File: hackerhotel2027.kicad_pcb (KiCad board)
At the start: 2 copper layers, 20 parts, among them J1 USB device, J2 USB host, U2 TPD4E05U06DQAR, Y1 32.768KHz

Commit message: Fill out all component LCSC numbers and fix footprint associations
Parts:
- removed C31: 100n, Capacitor_SMD:C_0402_1005Metric
- added C36: 4.7uF, Capacitor_SMD:C_0603_1608Metric, F.Cu at (174.6, 71.3)
- added C37: 1uF, Capacitor_SMD:C_0603_1608Metric, F.Cu at (174.6, 73.8)
- added C38: 1uF, Capacitor_SMD:C_0603_1608Metric, F.Cu at (174.6, 76.3)
- added C39: 1uF, Capacitor_SMD:C_0603_1608Metric, F.Cu at (174.6, 78.8)
- added C40: 1uF, Capacitor_SMD:C_0603_1608Metric, F.Cu at (174.6, 81.3)
- added C41: 1uF, Capacitor_SMD:C_0603_1608Metric, F.Cu at (178.6, 71.3)
- added C42: 1uF, Capacitor_SMD:C_0603_1608Metric, F.Cu at (178.6, 73.8)
- added C43: 1uF, Capacitor_SMD:C_0603_1608Metric, F.Cu at (178.6, 76.3)
- added C44: 1uF, Capacitor_SMD:C_0603_1608Metric, F.Cu at (178.6, 78.8)
- added C45: 470nF, Capacitor_SMD:C_0603_1608Metric, F.Cu at (178.6, 81.3)
- added D3: B0530WS, Diode_SMD:D_SOD-323, F.Cu at (187.3, 75.7)
- added D5: B0530WS, Diode_SMD:D_SOD-323, F.Cu at (187.3, 78.7)
- added D8: B0530WS, Diode_SMD:D_SOD-323, F.Cu at (187.3, 81.6)
- added FPC1: GT-F0501SR10-24S1101, lcsc:FPC-SMD_24P-P0.50_GT-F0501SR10-24S1101, F.Cu at (180.1, 67.0)
- added L1: 1.8n, Inductor_SMD:L_01005_0402Metric, F.Cu at (192.6, 69.4)
- added L9: 47uH, Inductor_SMD:L_1210_3225Metric, F.Cu at (183.4, 72.1)
- added Q2: AP2302B, lcsc:SOT-23-3_L2.9-W1.3-P1.90-LS2.4-BR, F.Cu at (182.8, 76.5)
- added R11: 2.2, Resistor_SMD:R_0805_2012Metric, F.Cu at (182.8, 80.2)
- added R12: 100k, Resistor_SMD:R_0402_1005Metric, F.Cu at (187.7, 71.0)
- added R13: 0, Resistor_SMD:R_0402_1005Metric, F.Cu at (187.7, 73.0)
- added U1: CH32V208CBU6_C5713556, ch32v208:QFN-48_L5.0-W5.0-P0.35-BL-EP-A, F.Cu at (209.1, 95.7)
- added Y2: 32MHz, Crystal:Crystal_SMD_3225-4Pin_3.2x2.5mm, F.Cu at (194.1, 66.3)
- C1, C2: value 22p -> 9p
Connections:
- J1 pad SH: (no net) -> GND

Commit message: Small tweaks & initial PCB work
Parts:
- AE2, C1, C2, C3, C32, C33, C34, C35, C36, C37, C38, C39, C4, C40, C41, C42, C43, C44, C45, C5, C6, C7, D3, D5, D8, FPC1, J1, J2, L1, L9, Q2, R1, R11, R12, R13, R2, R25, U1, U2, Y1, Y2: moved to B.Cu
- moved U1 235.6 mm to (3.88, -20.1), turned to 180 degrees
- moved R12 210.9 mm to (-9.88, -2.77), turned to 180 degrees
- moved L1 209.6 mm to (5.45, -25.0), turned to 90 degrees
- moved R11 208.8 mm to (-10.9, 2.23), turned to 180 degrees
- moved Y2 206.3 mm to (4.00, -14.0), turned to 180 degrees
- moved Q2 204.5 mm to (-4.88, -4.78), turned to 180 degrees
- moved C41 202.7 mm to (-10.9, -0.78), turned to 180 degrees
- moved D8 201.2 mm to (5.12, -3.77), turned to 180 degrees
- moved L9 198.8 mm to (0.12, -4.78), turned to 180 degrees
- moved R13 197.8 mm to (0.12, 10.2), turned to 180 degrees
- moved C36 197.6 mm to (2.00, -25.0), turned to 180 degrees
- moved C40 196.8 mm to (-6.88, 5.22), turned to 180 degrees
- moved J1 195.6 mm to (-32.0, 0.00), turned to 90 degrees
- moved R2 194.5 mm to (-25.0, 0.00), turned to 180 degrees
- moved D3 193.5 mm to (9.12, 0.23), turned to 180 degrees
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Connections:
- net BTN1 renamed PWR_BTN
- net BTN2 renamed T1
- U1 pad 11: unconnected-(U1-PA2/ADC2-Pad11) -> T2
- U1 pad 12: unconnected-(U1-PA3/ADC3-Pad12) -> T3
- U1 pad 13: unconnected-(U1-PA4/ADC4-Pad13) -> T4
- U1 pad 14: SPI_SCK -> T5
- U1 pad 15: SPI_MISO -> T6
- U1 pad 16: SPI_MOSI -> T7
- U1 pad 17: unconnected-(U1-PB0/ADC8-Pad17) -> T8
- U1 pad 18: unconnected-(U1-PB1/ADC9-Pad18) -> T9
- U1 pad 20: unconnected-(U1-PB10-Pad20) -> I2C2_SCL
- U1 pad 21: unconnected-(U1-PB11-Pad21) -> I2C2_SDA
- U1 pad 23: unconnected-(U1-PB12-Pad23) -> EPAPER_BUSY
- U1 pad 24: unconnected-(U1-PB13-Pad24) -> SPI_SCK
- U1 pad 25: unconnected-(U1-PB14-Pad25) -> SPI_MISO
- U1 pad 26: unconnected-(U1-PB15-Pad26) -> SPI_MOSI
- U1 pad 27: unconnected-(U1-PA8-Pad27) -> SPI_CS_EPAPER
- U1 pad 28: unconnected-(U1-PA9-Pad28) -> SPI_CS_FLASH
- U1 pad 29: unconnected-(U1-PA10-Pad29) -> EPAPER_DC
- U1 pad 37: unconnected-(U1-PA15-Pad37) -> LM4
- U1 pad 38: unconnected-(U1-PB3-Pad38) -> LM3
- U1 pad 39: unconnected-(U1-PB4-Pad39) -> LM2
- U1 pad 40: unconnected-(U1-PB5-Pad40) -> LM1
- U1 pad 43: unconnected-(U1-BOOT0-Pad43) -> BOOT
- U1 pad 44: unconnected-(U1-PB8-Pad44) -> I2C1_SCL
- U1 pad 45: unconnected-(U1-PB9-Pad45) -> I2C1_SDA
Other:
- board outline added: 70 x 70 mm

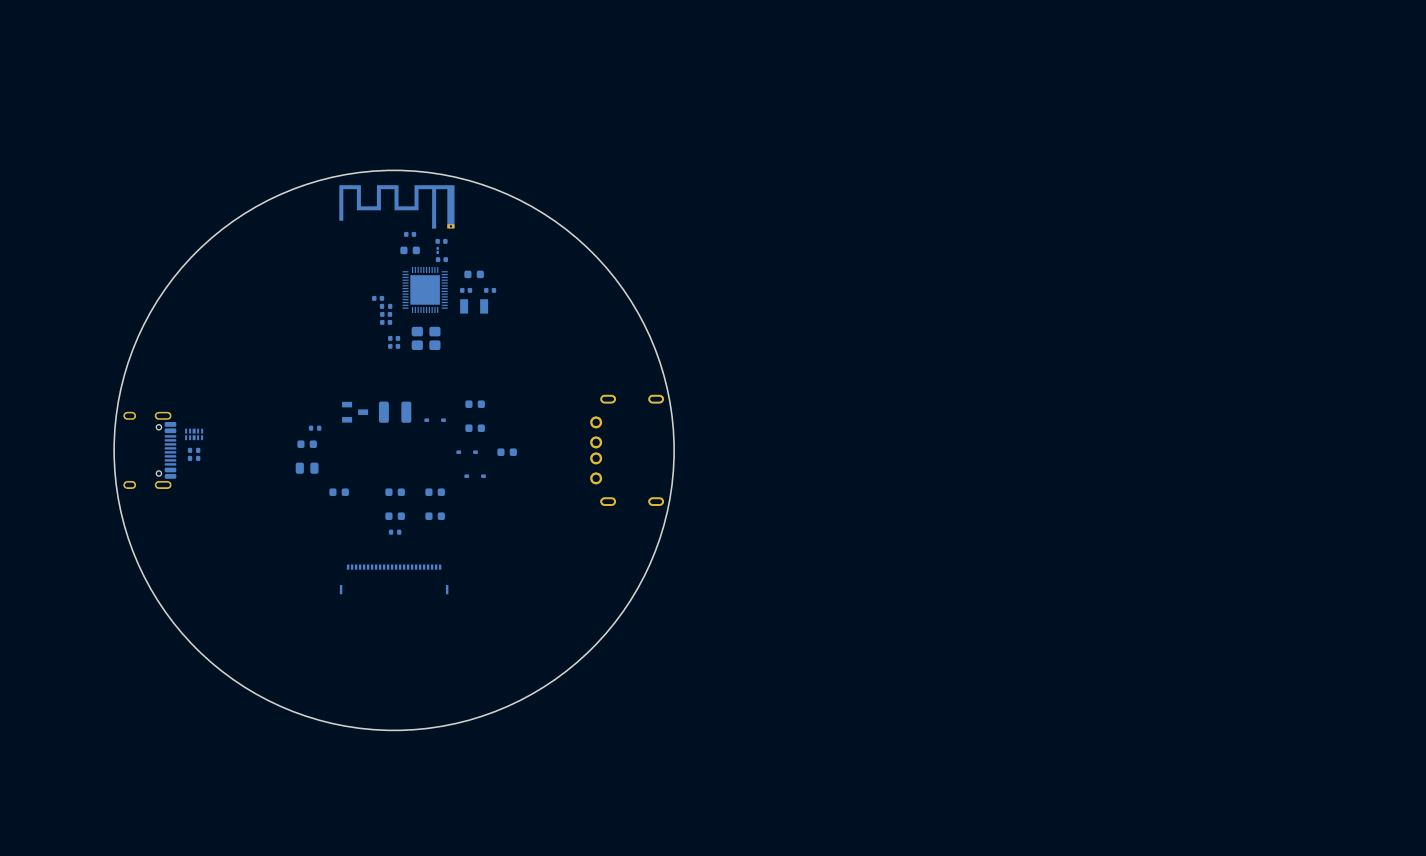
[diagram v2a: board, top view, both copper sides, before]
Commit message: Switch to WCH ledmatrix controller, add loads of LEDs
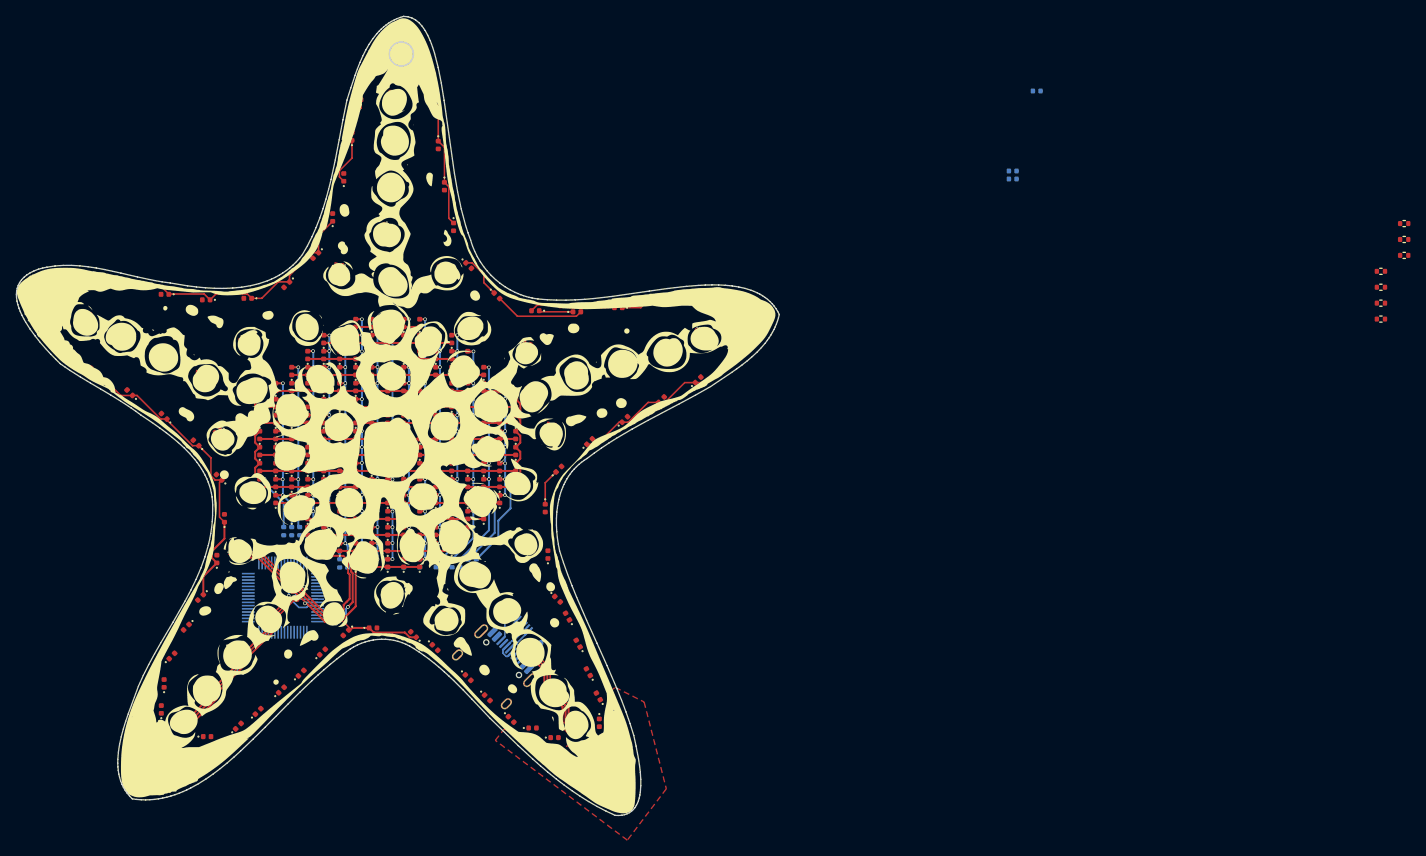
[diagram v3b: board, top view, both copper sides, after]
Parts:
- removed AE2: Antenna, RF_Antenna:Texas_SWRA117D_2.4GHz_Right
- removed the C1 at (12.0, -20.0)
- removed the C2 at (9.00, -20.0)
- removed the C3 at (0.00, -14.0)
- removed C32: 100n, Capacitor_SMD:C_0402_1005Metric
- removed C36: 4.7uF, Capacitor_SMD:C_0603_1608Metric
- removed C37, C38, C39, C40, C41, C42, C43, C44: 1uF, Capacitor_SMD:C_0603_1608Metric
- removed C4: ~, Capacitor_SMD:C_0402_1005Metric
- removed C45: 470nF, Capacitor_SMD:C_0603_1608Metric
- removed C5, C6: 1.8p, Capacitor_SMD:C_0402_1005Metric
- removed C7: 1u, Capacitor_SMD:C_0603_1608Metric
- removed FPC1: GT-F0501SR10-24S1101, lcsc:FPC-SMD_24P-P0.50_GT-F0501SR10-24S1101
- removed J2: USB host, library:USB-A-TH_JTJ-USB-A-F-10.0-010
- removed L1: 1.8n, Inductor_SMD:L_01005_0402Metric
- removed L9: 47uH, Inductor_SMD:L_1210_3225Metric
- removed Q2: AP2302B, lcsc:SOT-23-3_L2.9-W1.3-P1.90-LS2.4-BR
- removed the R25 at (-1.00, -18.0)
- removed Y1: 32.768KHz, Crystal:Crystal_SMD_3215-2Pin_3.2x1.5mm
- removed Y2: 32MHz, Crystal:Crystal_SMD_3225-4Pin_3.2x2.5mm
- added D1: LED, LED_SMD:LED_0402_1005Metric, F.Cu at (-23.4, 35.8)
- added D10: LED, LED_SMD:LED_0402_1005Metric, F.Cu at (-2.80, 14.1)
- added D100: LED, LED_SMD:LED_0402_1005Metric, F.Cu at (-16.8, 4.08)
- added D101: LED, LED_SMD:LED_0402_1005Metric, F.Cu at (-14.8, 4.08)
- added D102: LED, LED_SMD:LED_0402_1005Metric, F.Cu at (-12.8, 4.08)
- added D103: LED, LED_SMD:LED_0402_1005Metric, F.Cu at (-10.8, 4.08)
- added D104: LED, LED_SMD:LED_0402_1005Metric, F.Cu at (-8.80, 4.08)
- added D105: LED, LED_SMD:LED_0402_1005Metric, F.Cu at (-6.80, 4.08)
- added D106: LED, LED_SMD:LED_0402_1005Metric, F.Cu at (-4.80, 4.08)
- added D107: LED, LED_SMD:LED_0402_1005Metric, F.Cu at (-0.80, 4.08)
- added D108: LED, LED_SMD:LED_0402_1005Metric, F.Cu at (1.20, 4.08)
- added D109: LED, LED_SMD:LED_0402_1005Metric, F.Cu at (-2.80, 4.08)
- added D11: LED, LED_SMD:LED_0402_1005Metric, F.Cu at (3.20, 14.1)
- added D110: LED, LED_SMD:LED_0402_1005Metric, F.Cu at (3.20, 4.08)
- added D111: LED, LED_SMD:LED_0402_1005Metric, F.Cu at (5.20, 4.08)
- added D112: LED, LED_SMD:LED_0402_1005Metric, F.Cu at (7.20, 4.08)
- added D113: LED, LED_SMD:LED_0402_1005Metric, F.Cu at (9.20, 4.08)
- added D114: LED, LED_SMD:LED_0402_1005Metric, F.Cu at (11.2, 4.08)
- added D115: LED, LED_SMD:LED_0402_1005Metric, F.Cu at (13.2, 4.08)
- added D116: LED, LED_SMD:LED_0402_1005Metric, F.Cu at (15.2, 4.08)
- added D117: LED, LED_SMD:LED_0402_1005Metric, F.Cu at (-16.8, 2.08)
- added D118: LED, LED_SMD:LED_0402_1005Metric, F.Cu at (-14.8, 2.08)
- added D119: LED, LED_SMD:LED_0402_1005Metric, F.Cu at (-12.8, 2.08)
- added D12: LED, LED_SMD:LED_0402_1005Metric, F.Cu at (-6.02, 22.8)
- added D120: LED, LED_SMD:LED_0402_1005Metric, F.Cu at (-10.8, 2.08)
- added D121: LED, LED_SMD:LED_0402_1005Metric, F.Cu at (-8.80, 2.08)
- added D122: LED, LED_SMD:LED_0402_1005Metric, F.Cu at (-6.80, 2.08)
- added D123: LED, LED_SMD:LED_0402_1005Metric, F.Cu at (-4.80, 2.08)
- added D124: LED, LED_SMD:LED_0402_1005Metric, F.Cu at (-0.80, 2.08)
- added D125: LED, LED_SMD:LED_0402_1005Metric, F.Cu at (1.20, 2.08)
- added D126: LED, LED_SMD:LED_0402_1005Metric, F.Cu at (-2.80, 2.08)
- added D127: LED, LED_SMD:LED_0402_1005Metric, F.Cu at (3.20, 2.08)
- added D128: LED, LED_SMD:LED_0402_1005Metric, F.Cu at (5.20, 2.08)
- added D129: LED, LED_SMD:LED_0402_1005Metric, F.Cu at (7.20, 2.08)
- added D13: LED, LED_SMD:LED_0402_1005Metric, F.Cu at (-2.63, 22.2)
- added D130: LED, LED_SMD:LED_0402_1005Metric, F.Cu at (9.20, 2.08)
- added D131: LED, LED_SMD:LED_0402_1005Metric, F.Cu at (11.2, 2.08)
- added D132: LED, LED_SMD:LED_0402_1005Metric, F.Cu at (13.2, 2.08)
- added D133: LED, LED_SMD:LED_0402_1005Metric, F.Cu at (15.2, 2.08)
- added D134: LED, LED_SMD:LED_0402_1005Metric, F.Cu at (-16.8, 0.09)
- added D135: LED, LED_SMD:LED_0402_1005Metric, F.Cu at (-14.8, 0.09)
- added D136: LED, LED_SMD:LED_0402_1005Metric, F.Cu at (-12.8, 0.09)
- added D137: LED, LED_SMD:LED_0402_1005Metric, F.Cu at (-10.8, 0.09)
- added D138: LED, LED_SMD:LED_0402_1005Metric, F.Cu at (-8.80, 0.09)
- added D139: LED, LED_SMD:LED_0402_1005Metric, F.Cu at (-6.80, 0.09)
- added D14: LED, LED_SMD:LED_0402_1005Metric, F.Cu at (2.42, 23.0)
- added D140: LED, LED_SMD:LED_0402_1005Metric, F.Cu at (-4.80, 0.09)
- added D141: LED, LED_SMD:LED_0402_1005Metric, F.Cu at (-0.80, 0.09)
- added D142: LED, LED_SMD:LED_0402_1005Metric, F.Cu at (1.20, 0.09)
- added D143: LED, LED_SMD:LED_0402_1005Metric, F.Cu at (-2.80, 0.09)
- added D144: LED, LED_SMD:LED_0402_1005Metric, F.Cu at (3.20, 0.09)
- added D145: LED, LED_SMD:LED_0402_1005Metric, F.Cu at (5.20, 0.09)
- added D146: LED, LED_SMD:LED_0402_1005Metric, F.Cu at (7.20, 0.09)
- added D147: LED, LED_SMD:LED_0402_1005Metric, F.Cu at (9.20, 0.09)
- added D148: LED, LED_SMD:LED_0402_1005Metric, F.Cu at (11.2, 0.09)
- added D149: LED, LED_SMD:LED_0402_1005Metric, F.Cu at (13.2, 0.09)
- added D15: LED, LED_SMD:LED_0402_1005Metric, F.Cu at (17.3, 34.7)
- added D150: LED, LED_SMD:LED_0402_1005Metric, F.Cu at (15.2, 0.09)
- added D151: NH-B1515RGBA-GF, led:LED-SMD-4P-L1.6-W1.5_NH-B1515RGBA-GF, F.Cu at (38.6, -14.3)
- added D152: NH-B1515RGBA-GF, led:LED-SMD-4P-L1.6-W1.5_NH-B1515RGBA-GF, F.Cu at (34.1, -12.6)
- added D153: NH-B1515RGBA-GF, led:LED-SMD-4P-L1.6-W1.5_NH-B1515RGBA-GF, F.Cu at (28.4, -11.2)
- added D154: NH-B1515RGBA-GF, led:LED-SMD-4P-L1.6-W1.5_NH-B1515RGBA-GF, F.Cu at (22.7, -9.70)
- added D155: NH-B1515RGBA-GF, led:LED-SMD-4P-L1.6-W1.5_NH-B1515RGBA-GF, F.Cu at (17.3, -7.06)
- added D156: NH-B1515RGBA-GF, led:LED-SMD-4P-L1.6-W1.5_NH-B1515RGBA-GF, F.Cu at (19.5, -2.33)
- added D157: NH-B1515RGBA-GF, led:LED-SMD-4P-L1.6-W1.5_NH-B1515RGBA-GF, F.Cu at (16.4, -12.5)
- added D158: LED, LED_SMD:LED_0402_1005Metric, F.Cu at (-16.8, -3.92)
- added D159: LED, LED_SMD:LED_0402_1005Metric, F.Cu at (-14.8, -3.92)
- added D16: LED, LED_SMD:LED_0402_1005Metric, F.Cu at (20.1, 35.9)
- added D160: LED, LED_SMD:LED_0402_1005Metric, F.Cu at (-12.8, -3.92)
- added D161: LED, LED_SMD:LED_0402_1005Metric, F.Cu at (-10.8, -3.92)
- added D162: LED, LED_SMD:LED_0402_1005Metric, F.Cu at (-8.80, -3.92)
- added D163: LED, LED_SMD:LED_0402_1005Metric, F.Cu at (-6.80, -3.92)
- added D164: LED, LED_SMD:LED_0402_1005Metric, F.Cu at (-4.80, -3.92)
- added D165: LED, LED_SMD:LED_0402_1005Metric, F.Cu at (-0.80, -3.92)
- added D166: LED, LED_SMD:LED_0402_1005Metric, F.Cu at (1.20, -3.92)
- added D167: LED, LED_SMD:LED_0402_1005Metric, F.Cu at (-2.80, -3.92)
- added D168: LED, LED_SMD:LED_0402_1005Metric, F.Cu at (3.20, -3.92)
- added D169: LED, LED_SMD:LED_0402_1005Metric, F.Cu at (5.20, -3.92)
- added D17: LED, LED_SMD:LED_0402_1005Metric, F.Cu at (25.6, 34.0)
- added D170: LED, LED_SMD:LED_0402_1005Metric, F.Cu at (7.20, -3.92)
- added D171: LED, LED_SMD:LED_0402_1005Metric, F.Cu at (9.20, -3.92)
- added D172: LED, LED_SMD:LED_0402_1005Metric, F.Cu at (11.2, -3.92)
- added D173: LED, LED_SMD:LED_0402_1005Metric, F.Cu at (13.2, -3.92)
- added D174: LED, LED_SMD:LED_0402_1005Metric, F.Cu at (15.2, -3.92)
- added D175: LED, LED_SMD:LED_0402_1005Metric, F.Cu at (-16.8, -5.92)
- added D176: LED, LED_SMD:LED_0402_1005Metric, F.Cu at (-14.8, -5.92)
- added D177: LED, LED_SMD:LED_0402_1005Metric, F.Cu at (-12.8, -5.92)
- added D178: LED, LED_SMD:LED_0402_1005Metric, F.Cu at (-10.8, -5.92)
- added D179: LED, LED_SMD:LED_0402_1005Metric, F.Cu at (-8.80, -5.92)
- added D18: LED, LED_SMD:LED_0402_1005Metric, F.Cu at (25.5, 30.8)
- added D180: LED, LED_SMD:LED_0402_1005Metric, F.Cu at (-6.80, -5.92)
- added D181: LED, LED_SMD:LED_0402_1005Metric, F.Cu at (-4.80, -5.92)
- added D182: LED, LED_SMD:LED_0402_1005Metric, F.Cu at (-0.80, -5.92)
- added D183: LED, LED_SMD:LED_0402_1005Metric, F.Cu at (1.20, -5.92)
- added D184: LED, LED_SMD:LED_0402_1005Metric, F.Cu at (-2.80, -5.92)
- added D185: LED, LED_SMD:LED_0402_1005Metric, F.Cu at (3.20, -5.92)
- added D186: LED, LED_SMD:LED_0402_1005Metric, F.Cu at (5.20, -5.92)
- added D187: LED, LED_SMD:LED_0402_1005Metric, F.Cu at (7.20, -5.92)
- added D188: LED, LED_SMD:LED_0402_1005Metric, F.Cu at (9.20, -5.92)
- added D189: LED, LED_SMD:LED_0402_1005Metric, F.Cu at (11.2, -5.92)
- added D19: LED, LED_SMD:LED_0402_1005Metric, F.Cu at (24.3, 27.7)
- added D190: LED, LED_SMD:LED_0402_1005Metric, F.Cu at (13.2, -5.92)
- added D191: LED, LED_SMD:LED_0402_1005Metric, F.Cu at (15.2, -5.92)
- added D192: LED, LED_SMD:LED_0402_1005Metric, F.Cu at (12.8, -19.3)
- added D193: LED, LED_SMD:LED_0402_1005Metric, F.Cu at (-14.8, -7.92)
- added D194: LED, LED_SMD:LED_0402_1005Metric, F.Cu at (-12.8, -7.92)
- added D195: LED, LED_SMD:LED_0402_1005Metric, F.Cu at (-10.8, -7.92)
- added D196: LED, LED_SMD:LED_0402_1005Metric, F.Cu at (-8.80, -7.92)
- added D197: LED, LED_SMD:LED_0402_1005Metric, F.Cu at (-6.80, -7.92)
- added D198: LED, LED_SMD:LED_0402_1005Metric, F.Cu at (-4.80, -7.92)
- added D199: LED, LED_SMD:LED_0402_1005Metric, F.Cu at (-0.80, -7.92)
- added D2: LED, LED_SMD:LED_0402_1005Metric, F.Cu at (-19.5, 34.5)
- added D20: LED, LED_SMD:LED_0402_1005Metric, F.Cu at (23.0, 24.2)
- added D200: LED, LED_SMD:LED_0402_1005Metric, F.Cu at (1.20, -7.92)
- added D201: LED, LED_SMD:LED_0402_1005Metric, F.Cu at (-2.80, -7.92)
- added D202: LED, LED_SMD:LED_0402_1005Metric, F.Cu at (3.20, -7.92)
- added D203: LED, LED_SMD:LED_0402_1005Metric, F.Cu at (5.20, -7.92)
- added D204: LED, LED_SMD:LED_0402_1005Metric, F.Cu at (7.20, -7.92)
- added D205: LED, LED_SMD:LED_0402_1005Metric, F.Cu at (9.20, -7.92)
- added D206: LED, LED_SMD:LED_0402_1005Metric, F.Cu at (11.2, -7.92)
- added D207: LED, LED_SMD:LED_0402_1005Metric, F.Cu at (13.2, -7.92)
- added D208: LED, LED_SMD:LED_0402_1005Metric, F.Cu at (9.32, -23.1)
- added D209: NH-B1515RGBA-GF, led:LED-SMD-4P-L1.6-W1.5_NH-B1515RGBA-GF, F.Cu at (22.8, 34.2)
- added D21: LED, LED_SMD:LED_0402_1005Metric, F.Cu at (21.7, 20.8)
- added D210: NH-B1515RGBA-GF, led:LED-SMD-4P-L1.6-W1.5_NH-B1515RGBA-GF, F.Cu at (20.0, 30.2)
- added D211: NH-B1515RGBA-GF, led:LED-SMD-4P-L1.6-W1.5_NH-B1515RGBA-GF, F.Cu at (17.0, 25.0)
- added D212: NH-B1515RGBA-GF, led:LED-SMD-4P-L1.6-W1.5_NH-B1515RGBA-GF, F.Cu at (14.0, 20.0)
- added D213: NH-B1515RGBA-GF, led:LED-SMD-4P-L1.6-W1.5_NH-B1515RGBA-GF, F.Cu at (6.58, 21.2)
- added D214: NH-B1515RGBA-GF, led:LED-SMD-4P-L1.6-W1.5_NH-B1515RGBA-GF, F.Cu at (10.2, 15.8)
- added D215: NH-B1515RGBA-GF, led:LED-SMD-4P-L1.6-W1.5_NH-B1515RGBA-GF, F.Cu at (16.5, 11.8)
- added D216: LED, LED_SMD:LED_0402_1005Metric, F.Cu at (7.43, -27.9)
- added D217: LED, LED_SMD:LED_0402_1005Metric, F.Cu at (6.29, -33.0)
- added D218: LED, LED_SMD:LED_0402_1005Metric, F.Cu at (-12.8, -9.91)
- added D219: LED, LED_SMD:LED_0402_1005Metric, F.Cu at (-10.8, -9.91)
- added D22: LED, LED_SMD:LED_0402_1005Metric, F.Cu at (-8.80, 12.1)
- added D220: LED, LED_SMD:LED_0402_1005Metric, F.Cu at (-8.80, -9.91)
- added D221: LED, LED_SMD:LED_0402_1005Metric, F.Cu at (-6.80, -9.91)
- added D222: LED, LED_SMD:LED_0402_1005Metric, F.Cu at (-4.80, -9.91)
- added D223: LED, LED_SMD:LED_0402_1005Metric, F.Cu at (-0.80, -9.91)
- added D224: LED, LED_SMD:LED_0402_1005Metric, F.Cu at (1.20, -9.91)
- added D225: LED, LED_SMD:LED_0402_1005Metric, F.Cu at (-2.80, -9.91)
- added D226: LED, LED_SMD:LED_0402_1005Metric, F.Cu at (3.20, -9.91)
- added D227: LED, LED_SMD:LED_0402_1005Metric, F.Cu at (5.20, -9.91)
- added D228: LED, LED_SMD:LED_0402_1005Metric, F.Cu at (7.20, -9.91)
- added D229: LED, LED_SMD:LED_0402_1005Metric, F.Cu at (9.20, -9.91)
- added D23: LED, LED_SMD:LED_0402_1005Metric, F.Cu at (-6.80, 12.1)
- added D230: LED, LED_SMD:LED_0402_1005Metric, F.Cu at (11.2, -9.91)
- added D231: LED, LED_SMD:LED_0402_1005Metric, F.Cu at (5.52, -38.2)
- added D232: LED, LED_SMD:LED_0402_1005Metric, F.Cu at (4.79, -43.3)
- added D233: LED, LED_SMD:LED_0402_1005Metric, F.Cu at (3.81, -48.4)
- added D234: LED, LED_SMD:LED_0402_1005Metric, F.Cu at (1.32, -52.7)
- added D235: LED, LED_SMD:LED_0402_1005Metric, F.Cu at (-2.30, -49.2)
- added D236: LED, LED_SMD:LED_0402_1005Metric, F.Cu at (-10.8, -11.9)
- added D237: LED, LED_SMD:LED_0402_1005Metric, F.Cu at (-8.80, -11.9)
- added D238: LED, LED_SMD:LED_0402_1005Metric, F.Cu at (-6.80, -11.9)
- added D239: LED, LED_SMD:LED_0402_1005Metric, F.Cu at (-4.80, -11.9)
- added D24: LED, LED_SMD:LED_0402_1005Metric, F.Cu at (-4.80, 12.1)
- added D240: LED, LED_SMD:LED_0402_1005Metric, F.Cu at (-0.80, -11.9)
- added D241: LED, LED_SMD:LED_0402_1005Metric, F.Cu at (1.20, -11.9)
- added D242: LED, LED_SMD:LED_0402_1005Metric, F.Cu at (-2.80, -11.9)
- added D243: LED, LED_SMD:LED_0402_1005Metric, F.Cu at (3.20, -11.9)
- added D244: LED, LED_SMD:LED_0402_1005Metric, F.Cu at (5.20, -11.9)
- added D245: LED, LED_SMD:LED_0402_1005Metric, F.Cu at (7.20, -11.9)
- added D246: LED, LED_SMD:LED_0402_1005Metric, F.Cu at (9.20, -11.9)
- added D247: LED, LED_SMD:LED_0402_1005Metric, F.Cu at (-4.15, -44.3)
- added D248: LED, LED_SMD:LED_0402_1005Metric, F.Cu at (-5.27, -39.2)
- added D249: LED, LED_SMD:LED_0402_1005Metric, F.Cu at (-6.29, -34.1)
- added D25: LED, LED_SMD:LED_0402_1005Metric, F.Cu at (-0.80, 12.1)
- added D250: LED, LED_SMD:LED_0402_1005Metric, F.Cu at (-7.68, -29.1)
- added D251: LED, LED_SMD:LED_0402_1005Metric, F.Cu at (-9.80, -24.4)
- added D252: LED, LED_SMD:LED_0402_1005Metric, F.Cu at (-13.4, -20.7)
- added D253: LED, LED_SMD:LED_0402_1005Metric, F.Cu at (-18.3, -19.0)
- added D254: LED, LED_SMD:LED_0402_1005Metric, F.Cu at (-8.80, -13.9)
- added D255: LED, LED_SMD:LED_0402_1005Metric, F.Cu at (-6.80, -13.9)
- added D256: LED, LED_SMD:LED_0402_1005Metric, F.Cu at (-4.80, -13.9)
- added D257: LED, LED_SMD:LED_0402_1005Metric, F.Cu at (-0.80, -13.9)
- added D258: LED, LED_SMD:LED_0402_1005Metric, F.Cu at (1.20, -13.9)
- added D259: LED, LED_SMD:LED_0402_1005Metric, F.Cu at (-2.80, -13.9)
- added D26: LED, LED_SMD:LED_0402_1005Metric, F.Cu at (1.20, 12.1)
- added D260: LED, LED_SMD:LED_0402_1005Metric, F.Cu at (3.20, -13.9)
- added D261: LED, LED_SMD:LED_0402_1005Metric, F.Cu at (5.20, -13.9)
- added D262: LED, LED_SMD:LED_0402_1005Metric, F.Cu at (7.20, -13.9)
- added D263: LED, LED_SMD:LED_0402_1005Metric, F.Cu at (-23.5, -18.8)
- added D264: LED, LED_SMD:LED_0402_1005Metric, F.Cu at (-28.6, -19.5)
- added D265: LED, LED_SMD:LED_0402_1005Metric, F.Cu at (-33.8, -20.5)
- added D266: LED, LED_SMD:LED_0402_1005Metric, F.Cu at (-38.9, -21.5)
- added D267: NH-B1515RGBA-GF, led:LED-SMD-4P-L1.6-W1.5_NH-B1515RGBA-GF, F.Cu at (-38.7, -16.3)
- added D268: NH-B1515RGBA-GF, led:LED-SMD-4P-L1.6-W1.5_NH-B1515RGBA-GF, F.Cu at (-34.2, -14.6)
- added D269: NH-B1515RGBA-GF, led:LED-SMD-4P-L1.6-W1.5_NH-B1515RGBA-GF, F.Cu at (-29.0, -12.0)
- added D27: LED, LED_SMD:LED_0402_1005Metric, F.Cu at (-2.80, 12.1)
- added D270: NH-B1515RGBA-GF, led:LED-SMD-4P-L1.6-W1.5_NH-B1515RGBA-GF, F.Cu at (-23.7, -9.30)
- added D271: NH-B1515RGBA-GF, led:LED-SMD-4P-L1.6-W1.5_NH-B1515RGBA-GF, F.Cu at (-18.2, -13.7)
- added D272: NH-B1515RGBA-GF, led:LED-SMD-4P-L1.6-W1.5_NH-B1515RGBA-GF, F.Cu at (-17.9, -7.78)
- added D273: NH-B1515RGBA-GF, led:LED-SMD-4P-L1.6-W1.5_NH-B1515RGBA-GF, F.Cu at (-21.6, -1.70)
- added D274: LED, LED_SMD:LED_0402_1005Metric, F.Cu at (-43.6, -21.0)
- added D275: LED, LED_SMD:LED_0402_1005Metric, F.Cu at (-44.9, -17.0)
- added D276: LED, LED_SMD:LED_0402_1005Metric, F.Cu at (-41.7, -12.9)
- added D277: LED, LED_SMD:LED_0402_1005Metric, F.Cu at (-37.5, -9.90)
- added D278: LED, LED_SMD:LED_0402_1005Metric, F.Cu at (-33.0, -7.21)
- added D279: LED, LED_SMD:LED_0402_1005Metric, F.Cu at (-28.8, -4.26)
- added D28: LED, LED_SMD:LED_0402_1005Metric, F.Cu at (3.20, 12.1)
- added D280: LED, LED_SMD:LED_0402_1005Metric, F.Cu at (-4.80, -15.9)
- added D281: LED, LED_SMD:LED_0402_1005Metric, F.Cu at (-0.80, -15.9)
- added D282: LED, LED_SMD:LED_0402_1005Metric, F.Cu at (1.20, -15.9)
- added D283: LED, LED_SMD:LED_0402_1005Metric, F.Cu at (-2.80, -15.9)
- added D284: LED, LED_SMD:LED_0402_1005Metric, F.Cu at (3.20, -15.9)
- added D285: LED, LED_SMD:LED_0402_1005Metric, F.Cu at (-24.8, -0.93)
- added D286: LED, LED_SMD:LED_0402_1005Metric, F.Cu at (-21.9, 3.36)
- added D287: LED, LED_SMD:LED_0402_1005Metric, F.Cu at (-21.2, 8.48)
- added D288: LED, LED_SMD:LED_0402_1005Metric, F.Cu at (-22.2, 13.6)
- added D289: LED, LED_SMD:LED_0402_1005Metric, F.Cu at (-24.2, 18.4)
- added D29: LED, LED_SMD:LED_0402_1005Metric, F.Cu at (5.20, 12.1)
- added D290: LED, LED_SMD:LED_0402_1005Metric, F.Cu at (-26.0, 22.1)
- added D291: LED, LED_SMD:LED_0402_1005Metric, F.Cu at (-16.8, -1.92)
- added D292: LED, LED_SMD:LED_0402_1005Metric, F.Cu at (-14.8, -1.92)
- added D293: LED, LED_SMD:LED_0402_1005Metric, F.Cu at (-12.8, -1.92)
- added D294: LED, LED_SMD:LED_0402_1005Metric, F.Cu at (-10.8, -1.92)
- added D295: LED, LED_SMD:LED_0402_1005Metric, F.Cu at (-8.80, -1.92)
- added D296: LED, LED_SMD:LED_0402_1005Metric, F.Cu at (-6.80, -1.92)
- added D297: LED, LED_SMD:LED_0402_1005Metric, F.Cu at (-4.80, -1.92)
- added D298: LED, LED_SMD:LED_0402_1005Metric, F.Cu at (-0.80, -1.92)
- added D299: LED, LED_SMD:LED_0402_1005Metric, F.Cu at (1.20, -1.92)
- added D30: LED, LED_SMD:LED_0402_1005Metric, F.Cu at (7.20, 12.1)
- added D300: LED, LED_SMD:LED_0402_1005Metric, F.Cu at (-2.80, -1.92)
- added D301: LED, LED_SMD:LED_0402_1005Metric, F.Cu at (3.20, -1.92)
- added D302: LED, LED_SMD:LED_0402_1005Metric, F.Cu at (5.20, -1.92)
- added D303: LED, LED_SMD:LED_0402_1005Metric, F.Cu at (7.20, -1.92)
- added D304: LED, LED_SMD:LED_0402_1005Metric, F.Cu at (9.20, -1.92)
- added D305: LED, LED_SMD:LED_0402_1005Metric, F.Cu at (11.2, -1.92)
- added D306: LED, LED_SMD:LED_0402_1005Metric, F.Cu at (13.2, -1.92)
- added D307: LED, LED_SMD:LED_0402_1005Metric, F.Cu at (15.2, -1.92)
- added D308: LED, LED_SMD:LED_0402_1005Metric, F.Cu at (-27.8, 25.7)
- added D309: LED, LED_SMD:LED_0402_1005Metric, F.Cu at (-28.8, 29.1)
- added D31: LED, LED_SMD:LED_0402_1005Metric, F.Cu at (20.4, 18.6)
- added D310: LED, LED_SMD:LED_0402_1005Metric, F.Cu at (-29.1, 32.4)
- added D311: LED, LED_SMD:LED_0402_1005Metric, F.Cu at (14.6, 33.6)
- added D312: LED, LED_SMD:LED_0402_1005Metric, F.Cu at (11.7, 30.9)
- added D313: LED, LED_SMD:LED_0402_1005Metric, F.Cu at (9.25, 28.4)
- added D314: LED, LED_SMD:LED_0402_1005Metric, F.Cu at (5.12, 24.6)
- added D32: LED, LED_SMD:LED_0402_1005Metric, F.Cu at (19.2, 13.0)
- added D33: LED, LED_SMD:LED_0402_1005Metric, F.Cu at (18.9, 7.22)
- added D34: LED, LED_SMD:LED_0402_1005Metric, F.Cu at (20.6, 2.35)
- added D35: NH-B1515RGBA-GF, led:LED-SMD-4P-L1.6-W1.5_NH-B1515RGBA-GF, F.Cu at (-23.4, 30.0)
- added D36: NH-B1515RGBA-GF, led:LED-SMD-4P-L1.6-W1.5_NH-B1515RGBA-GF, F.Cu at (-26.2, 34.0)
- added D37: NH-B1515RGBA-GF, led:LED-SMD-4P-L1.6-W1.5_NH-B1515RGBA-GF, F.Cu at (-19.5, 25.6)
- added D38: NH-B1515RGBA-GF, led:LED-SMD-4P-L1.6-W1.5_NH-B1515RGBA-GF, F.Cu at (-15.5, 21.0)
- added D39: NH-B1515RGBA-GF, led:LED-SMD-4P-L1.6-W1.5_NH-B1515RGBA-GF, F.Cu at (-7.50, 20.5)
- added D4: LED, LED_SMD:LED_0402_1005Metric, F.Cu at (-17.0, 32.6)
- added D40: NH-B1515RGBA-GF, led:LED-SMD-4P-L1.6-W1.5_NH-B1515RGBA-GF, F.Cu at (-12.5, 15.8)
- added D41: NH-B1515RGBA-GF, led:LED-SMD-4P-L1.6-W1.5_NH-B1515RGBA-GF, F.Cu at (-19.5, 12.6)
- added D42: LED, LED_SMD:LED_0402_1005Metric, F.Cu at (24.4, -1.10)
- added D43: LED, LED_SMD:LED_0402_1005Metric, F.Cu at (28.8, -3.87)
- added D44: LED, LED_SMD:LED_0402_1005Metric, F.Cu at (33.4, -6.34)
- added D45: LED, LED_SMD:LED_0402_1005Metric, F.Cu at (-10.8, 10.1)
- added D46: LED, LED_SMD:LED_0402_1005Metric, F.Cu at (-8.80, 10.1)
- added D47: LED, LED_SMD:LED_0402_1005Metric, F.Cu at (-6.80, 10.1)
- added D48: LED, LED_SMD:LED_0402_1005Metric, F.Cu at (-4.80, 10.1)
- added D49: LED, LED_SMD:LED_0402_1005Metric, F.Cu at (-0.80, 10.1)
- added D50: LED, LED_SMD:LED_0402_1005Metric, F.Cu at (1.20, 10.1)
- added D51: LED, LED_SMD:LED_0402_1005Metric, F.Cu at (-2.80, 10.1)
- added D52: LED, LED_SMD:LED_0402_1005Metric, F.Cu at (3.20, 10.1)
- added D53: LED, LED_SMD:LED_0402_1005Metric, F.Cu at (5.20, 10.1)
- added D54: LED, LED_SMD:LED_0402_1005Metric, F.Cu at (7.20, 10.1)
- added D55: LED, LED_SMD:LED_0402_1005Metric, F.Cu at (9.20, 10.1)
- added D56: LED, LED_SMD:LED_0402_1005Metric, F.Cu at (38.0, -8.82)
- added D57: LED, LED_SMD:LED_0402_1005Metric, F.Cu at (42.3, -11.7)
- added D58: LED, LED_SMD:LED_0402_1005Metric, F.Cu at (45.9, -15.4)
- added D59: LED, LED_SMD:LED_0402_1005Metric, F.Cu at (43.5, -18.8)
- added D6: LED, LED_SMD:LED_0402_1005Metric, F.Cu at (-8.95, 25.2)
- added D60: LED, LED_SMD:LED_0402_1005Metric, F.Cu at (38.4, -19.1)
- added D61: LED, LED_SMD:LED_0402_1005Metric, F.Cu at (-12.8, 8.09)
- added D62: LED, LED_SMD:LED_0402_1005Metric, F.Cu at (-10.8, 8.09)
- added D63: LED, LED_SMD:LED_0402_1005Metric, F.Cu at (-8.80, 8.09)
- added D64: LED, LED_SMD:LED_0402_1005Metric, F.Cu at (-6.80, 8.09)
- added D65: LED, LED_SMD:LED_0402_1005Metric, F.Cu at (-4.80, 8.09)
- added D66: LED, LED_SMD:LED_0402_1005Metric, F.Cu at (-0.80, 8.09)
- added D67: LED, LED_SMD:LED_0402_1005Metric, F.Cu at (1.20, 8.09)
- added D68: LED, LED_SMD:LED_0402_1005Metric, F.Cu at (-2.80, 8.09)
- added D69: LED, LED_SMD:LED_0402_1005Metric, F.Cu at (3.20, 8.09)
- added D7: LED, LED_SMD:LED_0402_1005Metric, F.Cu at (-4.80, 14.1)
- added D70: LED, LED_SMD:LED_0402_1005Metric, F.Cu at (5.20, 8.09)
- added D71: LED, LED_SMD:LED_0402_1005Metric, F.Cu at (7.20, 8.09)
- added D72: LED, LED_SMD:LED_0402_1005Metric, F.Cu at (9.20, 8.09)
- added D73: LED, LED_SMD:LED_0402_1005Metric, F.Cu at (11.2, 8.09)
- added D74: LED, LED_SMD:LED_0402_1005Metric, F.Cu at (33.2, -18.6)
- added D75: LED, LED_SMD:LED_0402_1005Metric, F.Cu at (28.0, -17.8)
- added D76: LED, LED_SMD:LED_0402_1005Metric, F.Cu at (22.9, -17.3)
- added D77: LED, LED_SMD:LED_0402_1005Metric, F.Cu at (-14.8, 6.08)
- added D78: LED, LED_SMD:LED_0402_1005Metric, F.Cu at (-12.8, 6.08)
- added D79: LED, LED_SMD:LED_0402_1005Metric, F.Cu at (-10.8, 6.08)
- added D80: LED, LED_SMD:LED_0402_1005Metric, F.Cu at (-8.80, 6.08)
- added D81: LED, LED_SMD:LED_0402_1005Metric, F.Cu at (-6.80, 6.08)
- added D82: LED, LED_SMD:LED_0402_1005Metric, F.Cu at (-4.80, 6.08)
- added D83: LED, LED_SMD:LED_0402_1005Metric, F.Cu at (-0.80, 6.08)
- added D84: LED, LED_SMD:LED_0402_1005Metric, F.Cu at (1.20, 6.08)
- added D85: LED, LED_SMD:LED_0402_1005Metric, F.Cu at (-2.80, 6.08)
- added D86: LED, LED_SMD:LED_0402_1005Metric, F.Cu at (3.20, 6.08)
- added D87: LED, LED_SMD:LED_0402_1005Metric, F.Cu at (5.20, 6.08)
- added D88: LED, LED_SMD:LED_0402_1005Metric, F.Cu at (7.20, 6.08)
- added D89: LED, LED_SMD:LED_0402_1005Metric, F.Cu at (9.20, 6.08)
- added D9: LED, LED_SMD:LED_0402_1005Metric, F.Cu at (1.20, 14.1)
- added D90: LED, LED_SMD:LED_0402_1005Metric, F.Cu at (11.2, 6.08)
- added D91: LED, LED_SMD:LED_0402_1005Metric, F.Cu at (13.2, 6.08)
- added D92: LED, LED_SMD:LED_0402_1005Metric, F.Cu at (17.7, -17.5)
- added D93: NH-B1515RGBA-GF, led:LED-SMD-4P-L1.6-W1.5_NH-B1515RGBA-GF, F.Cu at (-0.09, -43.9)
- added D94: NH-B1515RGBA-GF, led:LED-SMD-4P-L1.6-W1.5_NH-B1515RGBA-GF, F.Cu at (-0.05, -39.0)
- added D95: NH-B1515RGBA-GF, led:LED-SMD-4P-L1.6-W1.5_NH-B1515RGBA-GF, F.Cu at (-0.52, -33.2)
- added D96: NH-B1515RGBA-GF, led:LED-SMD-4P-L1.6-W1.5_NH-B1515RGBA-GF, F.Cu at (-1.04, -27.3)
- added D97: NH-B1515RGBA-GF, led:LED-SMD-4P-L1.6-W1.5_NH-B1515RGBA-GF, F.Cu at (-7.00, -22.3)
- added D98: NH-B1515RGBA-GF, led:LED-SMD-4P-L1.6-W1.5_NH-B1515RGBA-GF, F.Cu at (-0.32, -21.3)
- added D99: NH-B1515RGBA-GF, led:LED-SMD-4P-L1.6-W1.5_NH-B1515RGBA-GF, F.Cu at (6.44, -22.5)
- added R1: R, Resistor_SMD:R_0402_1005Metric, B.Cu at (-13.8, 10.1)
- added R10: R, Resistor_SMD:R_0402_1005Metric, B.Cu at (-2.80, 14.1)
- added R14: R, Resistor_SMD:R_0402_1005Metric, B.Cu at (7.25, 14.1)
- added R15: R, Resistor_SMD:R_0402_1005Metric, B.Cu at (8.25, 14.1)
- added R16: R, Resistor_SMD:R_0402_1005Metric, B.Cu at (9.25, 14.1)
- added R17: R, Resistor_SMD:R_0402_1005Metric, B.Cu at (10.3, 14.1)
- added R18: R, Resistor_SMD:R_0402_1005Metric, F.Cu at (123.3, -22.4)
- added R19: R, Resistor_SMD:R_0402_1005Metric, F.Cu at (123.3, -20.4)
- added R2: R, Resistor_SMD:R_0402_1005Metric, B.Cu at (-12.8, 10.1)
- added R20: R, Resistor_SMD:R_0402_1005Metric, F.Cu at (123.3, -18.4)
- added R21: R, Resistor_SMD:R_0402_1005Metric, F.Cu at (123.3, -16.4)
- added R22: R, Resistor_SMD:R_0402_1005Metric, F.Cu at (126.3, -28.4)
- added R23: R, Resistor_SMD:R_0402_1005Metric, F.Cu at (126.3, -26.4)
- added R24: R, Resistor_SMD:R_0402_1005Metric, F.Cu at (126.3, -24.4)
- added R3: R, Resistor_SMD:R_0402_1005Metric, B.Cu at (-11.8, 10.1)
- added R4: R, Resistor_SMD:R_0402_1005Metric, B.Cu at (-10.8, 10.1)
- added R5: R, Resistor_SMD:R_0402_1005Metric, B.Cu at (-6.80, 14.1)
- added R6: R, Resistor_SMD:R_0402_1005Metric, B.Cu at (-5.80, 14.1)
- added R7: R, Resistor_SMD:R_0402_1005Metric, B.Cu at (-4.80, 14.1)
- added R8: R, Resistor_SMD:R_0402_1005Metric, B.Cu at (-0.80, 14.1)
- added R9: R, Resistor_SMD:R_0402_1005Metric, B.Cu at (1.20, 14.1)
- D3, D5, D8: value B0530WS -> LED; footprint Diode_SMD:D_SOD-323 -> LED_SMD:LED_0402_1005Metric; moved to F.Cu
- R11: value 2.2 -> R; footprint Resistor_SMD:R_0805_2012Metric -> Resistor_SMD:R_0402_1005Metric
- R12: value 100k -> R
- R13: value 0 -> R
- U1: value CH32V208CBU6_C5713556 -> CH643Q; footprint ch32v208:QFN-48_L5.0-W5.0-P0.35-BL-EP-A -> ch643:LQFP-64_L7.0-W7.0-P0.40-LS9.2-BL
- moved C1 80.4 mm to (77.3, -33.9)
- moved C2 80.4 mm to (80.3, -44.9)
- moved C3 80.4 mm to (77.3, -34.9)
- moved J1 51.9 mm to (11.7, 27.9), turned to 135 degrees
- moved R25 48.7 mm to (17.9, 24.0)
- moved U2 47.6 mm to (16.1, 21.9), turned to 135 degrees
- moved R26 44.0 mm to (13.8, 20.7), turned to -90 degrees
- moved U1 42.4 mm to (-13.9, 18.4), turned to 0 degrees
- moved D3 37.7 mm to (-14.1, 29.9), turned to 45 degrees
- moved D5 32.9 mm to (-11.6, 27.9), turned to 45 degrees
- moved R12 22.7 mm to (5.25, 14.1), turned to 90 degrees
- moved D8 18.8 mm to (-0.80, 14.1), turned to 90 degrees
- moved R11 18.4 mm to (3.20, 14.1), turned to 90 degrees
- moved R13 7.25 mm to (6.25, 14.1), turned to 90 degrees
- renumbered C35 to C1, C34 to C2, C33 to C3, R1 to R25, R2 to R26
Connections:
- net I2C1_SDA renamed SWIO
- D3 pad 1: Net-(D3-K) -> C1
- D3 pad 2: /display/PREVGL -> /R3b
- D5 pad 1: GND -> C1
- D5 pad 2: Net-(D3-K) -> /R5b
- D8 pad 1: /display/PREVGH -> C1
- D8 pad 2: Net-(D8-A) -> /R8b
- J1 pad A5: /CC1 -> CC1
- J1 pad A6: Net-(U1-PA12/USB1DP) -> USB_DP
- J1 pad A7: Net-(U1-PA11/USB1DM) -> USB_DN
- J1 pad B5: /CC2 -> CC2
- J1 pad B6: Net-(U1-PA12/USB1DP) -> USB_DP
- J1 pad B7: Net-(U1-PA11/USB1DM) -> USB_DN
- R11 pad 1: GND -> R11
- R11 pad 2: /display/RESE -> /R11b
- R12 pad 1: GND -> R12
- R12 pad 2: /display/GDR -> /R12b
- R13 pad 1: +3.3V -> R13
- R13 pad 2: Net-(C42-Pad2) -> /R13b
- R25 pad 2: /CC1 -> CC1
- R26 pad 2: /CC2 -> CC2
- U1 pad 1: unconnected-(U1-PC13/TAMPER_RTC-Pad1) -> GND
- U1 pad 10: T1 -> T2
- U1 pad 11: T2 -> T3
- U1 pad 12: T3 -> T4
- U1 pad 13: T4 -> R23
- U1 pad 14: T5 -> R24
- U1 pad 15: T6 -> R1
- U1 pad 16: T7 -> R2
- U1 pad 17: T8 -> R3
- U1 pad 18: T9 -> R4
- U1 pad 2: Net-(U1-PC14/OSC32IN) -> R16
- U1 pad 20: I2C2_SCL -> unconnected-(U1-PC5/SCK_/T1C1N_20-Pad20)
- U1 pad 21: I2C2_SDA -> R5
- U1 pad 22: +3.3V -> R6
- U1 pad 23: EPAPER_BUSY -> R7
- U1 pad 24: SPI_SCK -> R8
- U1 pad 25: SPI_MISO -> C1
- U1 pad 26: SPI_MOSI -> C2
- U1 pad 27: SPI_CS_EPAPER -> C3
- U1 pad 28: SPI_CS_FLASH -> C4
- U1 pad 29: EPAPER_DC -> C5
- U1 pad 3: Net-(U1-PC15/OSC32OUT) -> R17
- U1 pad 30: Net-(U1-PA11/USB1DM) -> GND
- U1 pad 31: Net-(U1-PA12/USB1DP) -> unconnected-(U1-VDD31-Pad31)
- U1 pad 32: SWDIO -> C6
- U1 pad 33: Net-(U1-VINTA) -> C7
- U1 pad 34: Net-(U1-ANT) -> C8
- U1 pad 35: GND -> C9
- U1 pad 36: SWCLK -> unconnected-(U1-PB16/TX3_/T2C1_36-Pad36)
- U1 pad 37: LM4 -> unconnected-(U1-PB17/T2C2_/RX3_37-Pad37)
- U1 pad 38: LM3 -> unconnected-(U1-PB18/T2C3_/CTS3_38-Pad38)
- U1 pad 39: LM2 -> unconnected-(U1-PB19/RTS3_/T2C4_39-Pad39)
- U1 pad 4: GND -> R18
- U1 pad 40: LM1 -> C10
- U1 pad 41: Net-(J2-D-) -> C11
- U1 pad 42: Net-(J2-D+) -> C12
- U1 pad 43: BOOT -> USB_DN
- U1 pad 44: I2C1_SCL -> USB_DP
- U1 pad 46: GND -> C13
- U1 pad 47: +3.3V -> SWCK
- U1 pad 48: unconnected-(U1-VBAT-Pad48) -> C14
- U1 pad 49: GND -> C15
- U1 pad 5: Net-(U1-OSC_IN) -> R19
- U1 pad 6: Net-(U1-OSC_OUT) -> R20
- U1 pad 7: Net-(U1-NRST) -> R21
- U1 pad 8: +3.3V -> R22
- U1 pad 9: PWR_BTN -> T1
- U2 pad 1: Net-(U1-PA11/USB1DM) -> USB_DN
- U2 pad 10: Net-(U1-PA11/USB1DM) -> USB_DN
- U2 pad 2: Net-(U1-PA12/USB1DP) -> USB_DP
- U2 pad 9: Net-(U1-PA12/USB1DP) -> USB_DP
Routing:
- net C3: track 0.00 -> 109.9 mm, vias 0 -> 2
- net C1: track 0.00 -> 72.1 mm, vias 0 -> 2
- net C2: track 0.00 -> 72.0 mm, vias 0 -> 3
- net C15: track 0.00 -> 64.2 mm
- net C14: track 0.00 -> 54.2 mm
- net C12: track 0.00 -> 53.7 mm
- net C13: track 0.00 -> 50.0 mm
- net C11: track 0.00 -> 47.6 mm
- net C10: track 0.00 -> 45.0 mm
- net /R7b: track 0.00 -> 43.3 mm, vias 0 -> 16
- net /R10b: track 0.00 -> 42.4 mm, vias 0 -> 16
- net /R11b: track 0.00 -> 41.6 mm, vias 0 -> 16
- net C4: track 0.00 -> 41.3 mm
- net /R9b: track 0.00 -> 41.1 mm, vias 0 -> 16
- net /R8b: track 0.00 -> 40.3 mm, vias 0 -> 16
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- added copper zone on In2.Cu, net GND
- added copper zone on F.Cu, net T1
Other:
- board size 70 x 70 mm -> 95.4 x 99.9 mm
- copper layers 2 -> 4
- board text added: "NH-B1515RGBA-GF"

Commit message: More routing
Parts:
- moved D235 8.44 mm to (-4.00, -40.9), turned to 90 degrees
- moved D74 8.23 mm to (40.8, -15.5), turned to 135 degrees
- moved D58 7.96 mm to (39.6, -10.6)
- moved D234 6.85 mm to (0.00, -46.0), turned to 0 degrees
- moved D59 5.32 mm to (38.7, -16.6)
- moved D274 4.72 mm to (-40.5, -17.5), turned to 45 degrees
- moved D233 4.50 mm to (3.00, -44.0), turned to 135 degrees
- moved D1 4.22 mm to (-27.6, 35.3), turned to 135 degrees
- moved D275 4.17 mm to (-41.2, -15.0), turned to 90 degrees
- moved D2 4.12 mm to (-23.4, 35.8), turned to 0 degrees
- moved D60 3.34 mm to (35.5, -17.4)
- moved D18 3.30 mm to (25.6, 34.0), turned to -90 degrees
- moved D19 3.27 mm to (25.5, 30.8)
- moved D4 3.08 mm to (-19.5, 34.5)
- moved D276 2.98 mm to (-38.8, -12.3)
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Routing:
- net Net-(D116-A): track 35.6 -> 117.5 mm, vias 1 -> 8
- net C5: track 32.3 -> 103.6 mm, vias 0 -> 3
- net C6: track 32.0 -> 100.5 mm, vias 0 -> 3
- net Net-(D115-A): track 29.9 -> 93.7 mm, vias 8 -> 13
- net C4: track 41.3 -> 102.7 mm, vias 0 -> 3
- net C13: track 50.0 -> 106.2 mm, vias 0 -> 2
- net /R2b: track 25.6 -> 80.7 mm, vias 8 -> 11
- net C7: track 32.0 -> 80.8 mm, vias 0 -> 5
- net /R1b: track 31.3 -> 77.6 mm, vias 1 -> 3
- net C14: track 54.2 -> 98.8 mm, vias 0 -> 2
- net C8: track 32.0 -> 75.7 mm, vias 0 -> 4
- net C9: track 32.0 -> 75.5 mm, vias 0 -> 2
- net C15: track 64.2 -> 104.3 mm, vias 0 -> 2
- net Net-(D311-A): track 0.00 -> 33.4 mm, vias 0 -> 2
- net Net-(D313-A): track 0.00 -> 32.6 mm, vias 0 -> 2
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
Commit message: LED routing
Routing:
- net /R1b: track 77.6 -> 149.2 mm, vias 3 -> 7
- net Net-(D115-A): track 93.7 -> 163.7 mm, vias 13 -> 15
- net /R4b: track 30.5 -> 90.1 mm, vias 12 -> 16
- net /R3b: track 57.7 -> 114.1 mm, vias 12 -> 13
- net Net-(D116-A): track 117.5 -> 165.8 mm, vias 8 -> 9
- net /R2b: track 80.7 -> 121.3 mm, vias 11 -> 13
- net Net-(D114-A): track 51.2 -> 86.2 mm
- net C12: track 51.1 -> 73.0 mm, vias 0 -> 2
- net C11: track 47.6 -> 61.7 mm
- net C4: track 102.7 -> 116.0 mm
- net C3: track 93.1 -> 104.9 mm
- net C14: track 98.8 -> 108.4 mm, vias 2 -> 4
- net C15: track 104.3 -> 113.5 mm
- net C2: track 72.0 -> 79.5 mm
- net C13: track 106.2 -> 113.3 mm
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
